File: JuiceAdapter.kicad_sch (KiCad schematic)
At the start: 6 parts, among them J1 Conn_01x04_Pin, J2 Conn_01x04_Pin, Q1 MMDT5401

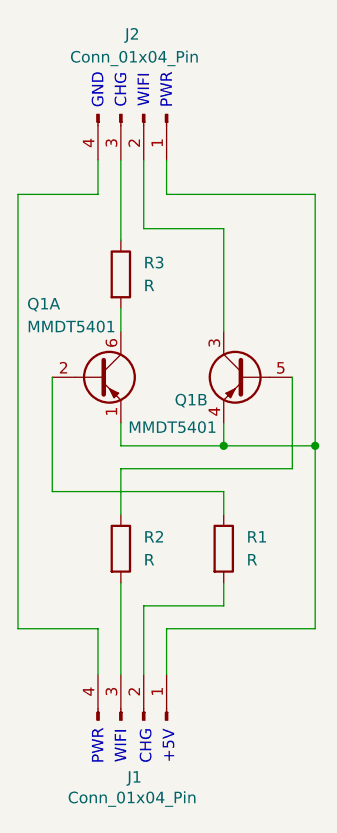
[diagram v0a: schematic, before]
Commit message: Clarified resistor values on schematic and PCB.
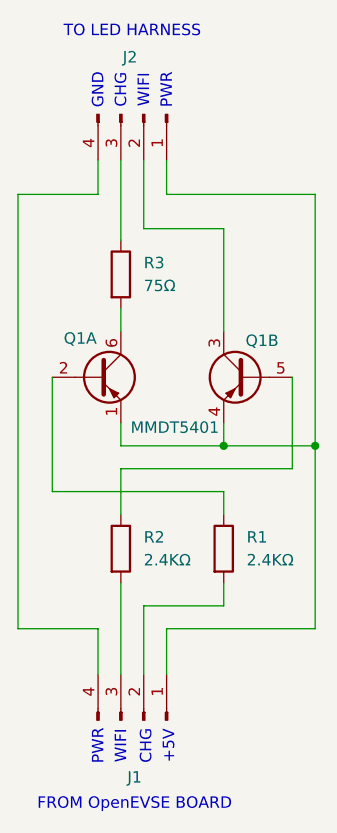
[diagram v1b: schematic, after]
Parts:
- R1, R2: value R -> 2.4KΩ
- R3: value R -> 75Ω
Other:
- note added: "FROM OpenEVSE BOARD"
- note added: "TO LED HARNESS"
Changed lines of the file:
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@@
+		)
+	)
+	(text "TO LED HARNESS"
+		(exclude_from_sim no)
+		(at 127 45.466 0)
+		(effects
+			(font
+				(size 1.27 1.27)
+			)
+		)
+	)
+	(text "FROM OpenEVSE BOARD"
+		(exclude_from_sim no)
+		(at 127.254 131.318 0)
+		(effects
+			(font
+				(size 1.27 1.27)
+			)
 		)
 	)
@@
 		(dnp no)
 		(property "Reference" "Q1"
-			(at 115.316 75.692 0)
+			(at 119.38 79.502 0)
 			(effects
 				(font
@@
 				)
 				(justify left)
+				(hide yes)
 			)
 		)
@@
 			)
 		)
-		(property "Value" "R"
+		(property "Value" "2.4KΩ"
 			(at 128.27 104.1399 0)
 			(effects
@@
 		(dnp no)
 		(property "Reference" "J2"
-			(at 127 45.72 90)
+			(at 126.746 48.26 90)
 			(effects
 				(font
@@
 					(size 1.27 1.27)
 				)
+				(hide yes)
 			)
 		)
@@
 			)
 		)
-		(property "Value" "R"
+		(property "Value" "2.4KΩ"
 			(at 139.7 104.1399 0)
 			(effects
@@
 					(size 1.27 1.27)
 				)
+				(hide yes)
 			)
 		)
@@
 		(dnp no)
 		(property "Reference" "Q1"
-			(at 135.382 86.36 0)
+			(at 143.256 79.756 0)
 			(effects
 				(font
@@
 		)
 		(property "Value" "MMDT5401"
-			(at 136.398 89.408 0)
+			(at 136.652 89.408 0)
 			(effects
 				(font
@@
 			)
 		)
-		(property "Value" "R"
+		(property "Value" "75Ω"
 			(at 128.27 73.6599 0)
 			(effects
